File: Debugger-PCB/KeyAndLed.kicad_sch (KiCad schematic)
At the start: 13 parts, among them SW3 SW_Push, SW4 SW_Push, SW5 SW_Push

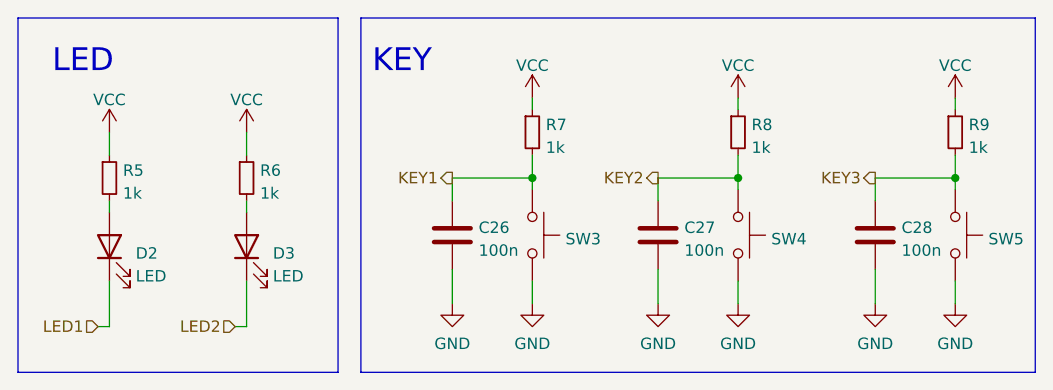
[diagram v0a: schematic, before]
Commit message: fix some details of PCB
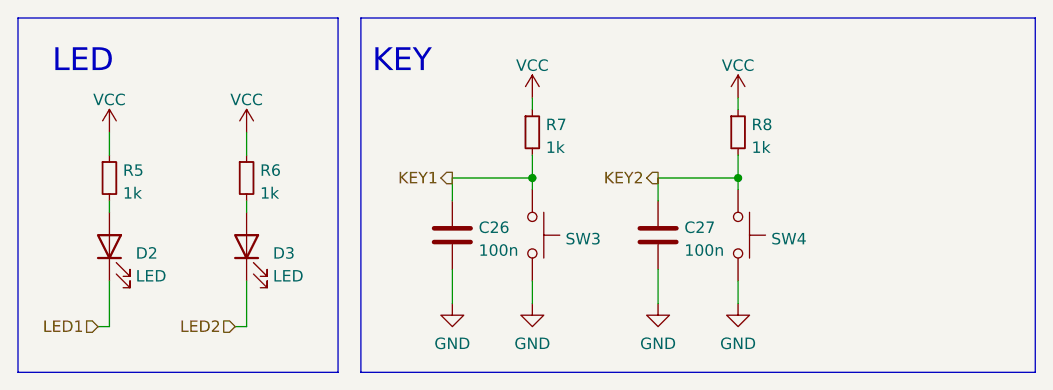
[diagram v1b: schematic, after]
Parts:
- removed C28: 100n, Capacitor_SMD:C_0603_1608Metric, symbol Device:C
- removed R9: 1k, Resistor_SMD:R_0603_1608Metric, symbol Device:R_Small
- removed SW5: SW_Push, MyLib:SW_YD-3410, symbol Switch:SW_Push
- SW3, SW4: footprint MyLib:SW_YD-3410 -> debugger:button
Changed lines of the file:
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@@
   (junction (at 199.39 93.98) (diameter 0) (color 0 0 0 0)
   )
-  (junction (at 223.52 93.98) (diameter 0) (color 0 0 0 0)
-  )
   (junction (at 176.53 93.98) (diameter 0) (color 0 0 0 0)
   )
@@
     (stroke (width 0) (type default) (color 0 0 0 0))
   )
-  (wire (pts (xy 214.63 93.98) (xy 223.52 93.98))
-    (stroke (width 0) (type default) (color 0 0 0 0))
-  )
   (wire (pts (xy 129.54 110.49) (xy 129.54 105.41))
     (stroke (width 0) (type default) (color 0 0 0 0))
@@
     (stroke (width 0) (type default) (color 0 0 0 0))
   )
-  (wire (pts (xy 223.52 93.98) (xy 223.52 95.25))
-    (stroke (width 0) (type default) (color 0 0 0 0))
-  )
   (wire (pts (xy 199.39 93.98) (xy 199.39 95.25))
     (stroke (width 0) (type default) (color 0 0 0 0))
   )
-  (wire (pts (xy 223.52 85.09) (xy 223.52 86.36))
-    (stroke (width 0) (type default) (color 0 0 0 0))
-  )
   (wire (pts (xy 129.54 96.52) (xy 129.54 97.79))
     (stroke (width 0) (type default) (color 0 0 0 0))
@@
     (stroke (width 0) (type default) (color 0 0 0 0))
   )
-  (wire (pts (xy 214.63 104.14) (xy 214.63 107.95))
-    (stroke (width 0) (type default) (color 0 0 0 0))
-  )
   (wire (pts (xy 176.53 105.41) (xy 176.53 107.95))
     (stroke (width 0) (type default) (color 0 0 0 0))
@@
     (stroke (width 0) (type default) (color 0 0 0 0))
   )
-  (wire (pts (xy 223.52 105.41) (xy 223.52 107.95))
-    (stroke (width 0) (type default) (color 0 0 0 0))
-  )
   (polyline (pts (xy 119.38 115.57) (xy 154.94 115.57))
     (stroke (width 0) (type default) (color 0 0 0 0))
@@
     (stroke (width 0) (type default) (color 0 0 0 0))
   )
-  (wire (pts (xy 214.63 96.52) (xy 214.63 93.98))
-    (stroke (width 0) (type default) (color 0 0 0 0))
-  )
   (wire (pts (xy 199.39 91.44) (xy 199.39 93.98))
-    (stroke (width 0) (type default) (color 0 0 0 0))
-  )
-  (wire (pts (xy 223.52 91.44) (xy 223.52 93.98))
     (stroke (width 0) (type default) (color 0 0 0 0))
   )
@@
     (effects (font (size 1.27 1.27)) (justify right))
   )
-  (hierarchical_label "KEY3" (shape output) (at 214.63 93.98 180)
-    (effects (font (size 1.27 1.27)) (justify right))
-  )
   (hierarchical_label "KEY1" (shape output) (at 167.64 93.98 180)
     (effects (font (size 1.27 1.27)) (justify right))
@@
     (effects (font (size 1.27 1.27)) (justify right))
   )
-  (symbol (lib_id "Device:R_Small") (at 223.52 88.9 0) (unit 1)
-    (in_bom yes) (on_board yes) (fields_autoplaced)
-    (property "Reference" "R9" (id 0) (at 225.0186 88.0653 0)
-      (effects (font (size 1.27 1.27)) (justify left))
-    )
-    (property "Value" "1k" (id 1) (at 225.0186 90.6022 0)
-      (effects (font (size 1.27 1.27)) (justify left))
-    )
-    (property "Footprint" "Resistor_SMD:R_0603_1608Metric" (id 2) (at 223.52 88.9 0)
-      (effects (font (size 1.27 1.27)) hide)
-    )
-    (property "Datasheet" "~" (id 3) (at 223.52 88.9 0)
-      (effects (font (size 1.27 1.27)) hide)
-    )
-    (pin "1")
-    (pin "2")
-  )
   (symbol (lib_id "Switch:SW_Push") (at 176.53 100.33 270) (mirror x) (unit 1)
     (in_bom yes) (on_board yes) (fields_autoplaced)
@@
       (effects (font (size 1.27 1.27)) (justify right) hide)
     )
-    (property "Footprint" "MyLib:SW_YD-3410" (id 2) (at 181.61 100.33 0)
+    (property "Footprint" "debugger:button" (id 2) (at 181.61 100.33 0)
       (effects (font (size 1.27 1.27)) hide)
     )
@@
     (pin "1")
     (pin "2")
-  )
-  (symbol (lib_id "power:GND") (at 223.52 107.95 0) (unit 1)
-    (in_bom yes) (on_board yes) (fields_autoplaced)
-    (property "Reference" "#PWR064" (id 0) (at 223.52 114.3 0)
-      (effects (font (size 1.27 1.27)) hide)
-    )
-    (property "Value" "GND" (id 1) (at 223.52 112.3934 0))
-    (property "Footprint" "" (id 2) (at 223.52 107.95 0)
-      (effects (font (size 1.27 1.27)) hide)
-    )
-    (property "Datasheet" "" (id 3) (at 223.52 107.95 0)
-      (effects (font (size 1.27 1.27)) hide)
-    )
-    (pin "1")
   )
   (symbol (lib_id "power:GND") (at 199.39 107.95 0) (unit 1)
@@
     (pin "1")
   )
-  (symbol (lib_id "power:GND") (at 214.63 107.95 0) (unit 1)
-    (in_bom yes) (on_board yes) (fields_autoplaced)
-    (property "Reference" "#PWR063" (id 0) (at 214.63 114.3 0)
-      (effects (font (size 1.27 1.27)) hide)
-    )
-    (property "Value" "GND" (id 1) (at 214.63 112.3934 0))
-    (property "Footprint" "" (id 2) (at 214.63 107.95 0)
-      (effects (font (size 1.27 1.27)) hide)
-    )
-    (property "Datasheet" "" (id 3) (at 214.63 107.95 0)
-      (effects (font (size 1.27 1.27)) hide)
-    )
-    (pin "1")
-  )
   (symbol (lib_id "power:VCC") (at 129.54 88.9 0) (unit 1)
     (in_bom yes) (on_board yes) (fields_autoplaced)
@@
       (effects (font (size 1.27 1.27)) (justify right) hide)
     )
-    (property "Footprint" "MyLib:SW_YD-3410" (id 2) (at 204.47 100.33 0)
+    (property "Footprint" "debugger:button" (id 2) (at 204.47 100.33 0)
       (effects (font (size 1.27 1.27)) hide)
     )
@@
     (pin "2")
   )
-  (symbol (lib_id "Device:C") (at 214.63 100.33 0) (unit 1)
-    (in_bom yes) (on_board yes)
-    (property "Reference" "C28" (id 0) (at 217.551 99.4953 0)
-      (effects (font (size 1.27 1.27)) (justify left))
-    )
-    (property "Value" "100n" (id 1) (at 217.551 102.0322 0)
-      (effects (font (size 1.27 1.27)) (justify left))
-    )
-    (property "Footprint" "Capacitor_SMD:C_0603_1608Metric" (id 2) (at 215.5952 104.14 0)
-      (effects (font (size 1.27 1.27)) hide)
-    )
-    (property "Datasheet" "~" (id 3) (at 214.63 100.33 0)
-      (effects (font (size 1.27 1.27)) hide)
-    )
-    (pin "1")
-    (pin "2")
-  )
   (symbol (lib_id "power:GND") (at 167.64 107.95 0) (unit 1)
     (in_bom yes) (on_board yes) (fields_autoplaced)
@@
     (pin "2")
   )
-  (symbol (lib_id "Switch:SW_Push") (at 223.52 100.33 270) (mirror x) (unit 1)
-    (in_bom yes) (on_board yes) (fields_autoplaced)
-    (property "Reference" "SW5" (id 0) (at 227.203 100.7638 90)
-      (effects (font (size 1.27 1.27)) (justify left))
-    )
-    (property "Value" "SW_Push" (id 1) (at 222.377 102.0322 90)
-      (effects (font (size 1.27 1.27)) (justify right) hide)
-    )
-    (property "Footprint" "MyLib:SW_YD-3410" (id 2) (at 228.6 100.33 0)
-      (effects (font (size 1.27 1.27)) hide)
-    )
-    (property "Datasheet" "~" (id 3) (at 228.6 100.33 0)
-      (effects (font (size 1.27 1.27)) hide)
-    )
-    (pin "1")
-    (pin "2")
-  )
   (symbol (lib_id "Device:R_Small") (at 144.78 93.98 0) (unit 1)
     (in_bom yes) (on_board yes) (fields_autoplaced)
@@
       (effects (font (size 1.27 1.27)) hide)
     )
-    (pin "1")
-  )
-  (symbol (lib_id "power:VCC") (at 223.52 85.09 0) (unit 1)
-    (in_bom yes) (on_board yes) (fields_autoplaced)
-    (property "Reference" "#PWR058" (id 0) (at 223.52 88.9 0)
-      (effects (font (size 1.27 1.27)) hide)
-    )
-    (property "Value" "VCC" (id 1) (at 223.52 81.4855 0))
-    (property "Footprint" "" (id 2) (at 223.52 85.09 0)
-      (effects (font (size 1.27 1.27)) hide)
-    )
-    (property "Datasheet" "" (id 3) (at 223.52 85.09 0)
-      (effects (font (size 1.27 1.27)) hide)
-    )

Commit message: change the file name debugger-code into debugger_code_f103. Change the stm32f103rct6 into stm32f407vet6. Add file debugger_code_f407
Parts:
- added C32: 100n, Capacitor_SMD:C_0603_1608Metric, symbol Device:C
- added R12: 1k, Resistor_SMD:R_0603_1608Metric, symbol Device:R_Small
- added SW3: SW_Push, debugger:button, symbol Switch:SW_Push
- renumbered C26 to C30, C27 to C31, R7 to R10, R8 to R11, R5 to R8, R6 to R9, SW3 to SW1, SW4 to SW2
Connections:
- net GND: now also C32.2, SW3.1
- net VCC: now also R12.1
- new net KEY3: C32.1, R12.2, SW3.2
